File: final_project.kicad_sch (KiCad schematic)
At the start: 1 part, among them U1 ATmega328-P

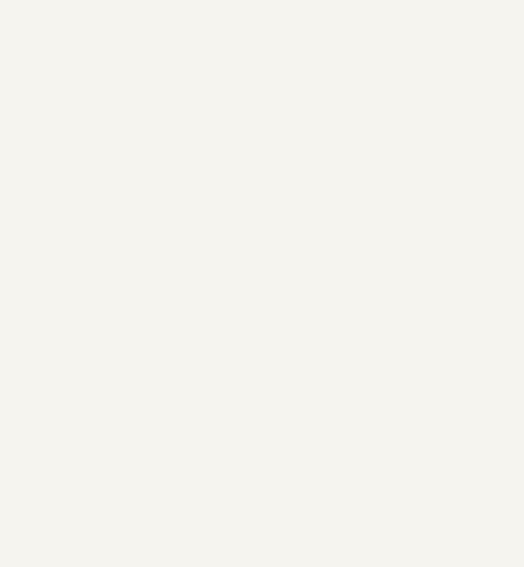
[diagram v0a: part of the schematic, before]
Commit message: Added SGP30 Sensor
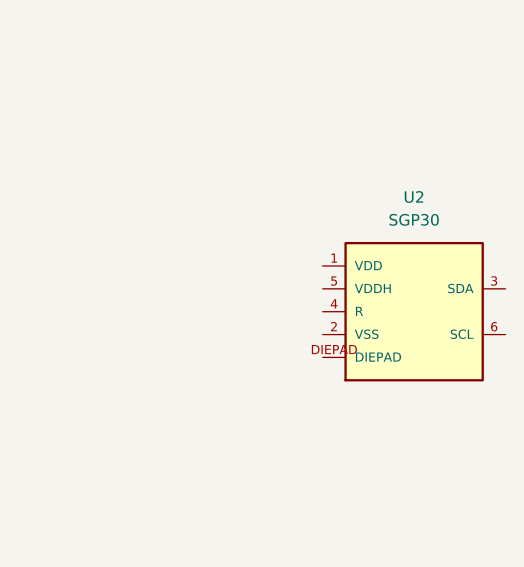
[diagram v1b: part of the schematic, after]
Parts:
- added U2: SGP30, SGP30:SGP30, symbol SGP30:SGP30
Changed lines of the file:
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@@
 	(paper "A4")
+	(symbol
+		(lib_id "SGP30:SGP30")
+		(at 158.75 87.63 0)
+		(unit 1)
+		(exclude_from_sim no)
+		(in_bom yes)
+		(on_board yes)
+		(dnp no)
+		(fields_autoplaced yes)
+		(property "Reference" "U2"
+			(at 158.75 74.93 0)
+			(effects
+				(font
+					(size 1.27 1.27)
+				)
+			)
+		)
+		(property "Value" "SGP30"
+			(at 158.75 77.47 0)
+			(effects
+				(font
+					(size 1.27 1.27)
+				)
+			)
+		)
+		(property "Footprint" "SGP30:SGP30"
+			(at 158.75 87.63 0)
+			(effects
+				(font
+					(size 1.27 1.27)
+				)
+				(justify bottom)
+				(hide yes)
+			)
+		)
+		(property "Datasheet" ""
+			(at 158.75 87.63 0)
+			(effects
+				(font
+					(size 1.27 1.27)
+				)
+				(hide yes)
+			)
+		)
+		(property "Description" ""
+			(at 158.75 87.63 0)
+			(effects
+				(font
+					(size 1.27 1.27)
+				)
+				(hide yes)
+			)
+		)
+		(property "MF" "Sensirion AG"
+			(at 158.75 87.63 0)
+			(effects
+				(font
+					(size 1.27 1.27)
+				)
+				(justify bottom)
+				(hide yes)
+			)
+		)
+		(property "Description_1" "SGP30, SHTC1 Air Quality, Humidity, Temperature Sensor Arduino Platform Evaluation Expansion Board"
+			(at 158.75 87.63 0)
+			(effects
+				(font
+					(size 1.27 1.27)
+				)
+				(justify bottom)
+				(hide yes)
+			)
+		)
+		(property "Package" "None"
+			(at 158.75 87.63 0)
+			(effects
+				(font
+					(size 1.27 1.27)
+				)
+				(justify bottom)
+				(hide yes)
+			)
+		)
+		(property "Price" "None"
+			(at 158.75 87.63 0)
+			(effects
+				(font
+					(size 1.27 1.27)
+				)
+				(justify bottom)
+				(hide yes)
+			)
+		)
+		(property "Check_prices" "https://www.snapeda.com/parts/SGP30/Sensirion/view-part/?ref=eda"
+			(at 158.75 87.63 0)
+			(effects
+				(font
+					(size 1.27 1.27)
+				)
+				(justify bottom)
+				(hide yes)
+			)
+		)
+		(property "VALUE" "SGP30"
+			(at 158.75 87.63 0)
+			(effects
+				(font
+					(size 1.27 1.27)
+				)
+				(justify bottom)
+				(hide yes)
+			)
+		)
+		(property "SnapEDA_Link" "https://www.snapeda.com/parts/SGP30/Sensirion/view-part/?ref=snap"
+			(at 158.75 87.63 0)
+			(effects
+				(font
+					(size 1.27 1.27)
+				)
+				(justify bottom)
+				(hide yes)
+			)
+		)
+		(property "PROD_ID" "IC-14776"
+			(at 158.75 87.63 0)
+			(effects
+				(font
+					(size 1.27 1.27)
+				)
+				(justify bottom)
+				(hide yes)
+			)
+		)
+		(property "Availability" "Not in stock"
+			(at 158.75 87.63 0)
+			(effects
+				(font
+					(size 1.27 1.27)
+				)
+				(justify bottom)
+				(hide yes)
+			)
+		)
+		(property "MP" "SGP30"
+			(at 158.75 87.63 0)
+			(effects
+				(font
+					(size 1.27 1.27)
+				)
+				(justify bottom)
+				(hide yes)
+			)
+		)
+		(pin "2"
+		)
+		(pin "3"
+		)
+		(pin "5"
+		)
+		(pin "1"
+		)
+		(pin "4"
+		)
+		(pin "DIEPAD"
+		)
+		(pin "6"
+		)
+		(instances
+			(project ""
+				(path "/69077819-e109-4340-8082-9c11186228b7"
+					(reference "U2")
+					(unit 1)
+				)
+			)
+		)
+	)
 	(symbol
 		(lib_id "MCU_Microchip_ATmega:ATmega328-P")

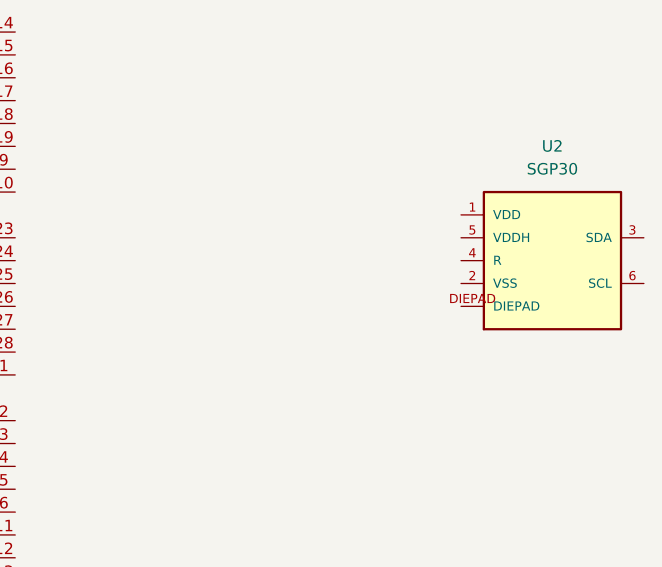
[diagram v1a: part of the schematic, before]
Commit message: Added GND to SGP30 sensor
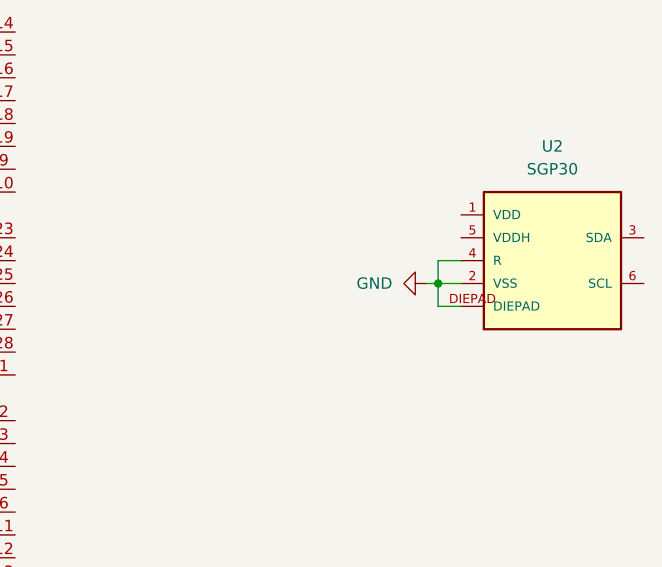
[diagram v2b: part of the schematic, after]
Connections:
- net GND: now reaches U2.2 (VSS)
- net GND: now also U2.4 (R), U2.DIEPAD
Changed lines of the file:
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@@
 	(generator_version "9.0")
 	(paper "A4")
+	(junction
+		(at 146.05 90.17)
+		(diameter 0)
+		(color 0 0 0 0)
+	)
+	(wire
+		(pts
+			(xy 146.05 90.17) (xy 148.59 90.17)
+		)
+		(stroke
+			(width 0)
+			(type default)
+		)
+	)
+	(wire
+		(pts
+			(xy 146.05 87.63) (xy 148.59 87.63)
+		)
+		(stroke
+			(width 0)
+			(type default)
+		)
+	)
+	(wire
+		(pts
+			(xy 146.05 90.17) (xy 146.05 92.71)
+		)
+		(stroke
+			(width 0)
+			(type default)
+		)
+	)
+	(wire
+		(pts
+			(xy 146.05 92.71) (xy 148.59 92.71)
+		)
+		(stroke
+			(width 0)
+			(type default)
+		)
+	)
+	(wire
+		(pts
+			(xy 146.05 90.17) (xy 146.05 87.63)
+		)
+		(stroke
+			(width 0)
+			(type default)
+		)
+	)
+	(wire
+		(pts
+			(xy 144.78 90.17) (xy 146.05 90.17)
+		)
+		(stroke
+			(width 0)
+			(type default)
+		)
+	)
+	(symbol
+		(lib_id "power:GND")
+		(at 144.78 90.17 270)
+		(unit 1)
+		(exclude_from_sim no)
+		(in_bom yes)
+		(on_board yes)
+		(dnp no)
+		(fields_autoplaced yes)
+		(property "Reference" "#PWR01"
+			(at 138.43 90.17 0)
+			(effects
+				(font
+					(size 1.27 1.27)
+				)
+				(hide yes)
+			)
+		)
+		(property "Value" "GND"
+			(at 140.97 90.1699 90)
+			(effects
+				(font
+					(size 1.27 1.27)
+				)
+				(justify right)
+			)
+		)
+		(property "Footprint" ""
+			(at 144.78 90.17 0)
+			(effects
+				(font
+					(size 1.27 1.27)
+				)
+				(hide yes)
+			)
+		)
+		(property "Datasheet" ""
+			(at 144.78 90.17 0)
+			(effects
+				(font
+					(size 1.27 1.27)
+				)
+				(hide yes)
+			)
+		)
+		(property "Description" "Power symbol creates a global label with name \"GND\" , ground"
+			(at 144.78 90.17 0)
+			(effects
+				(font
+					(size 1.27 1.27)
+				)
+				(hide yes)
+			)
+		)
+		(pin "1"
+		)
+		(instances
+			(project ""
+				(path "/69077819-e109-4340-8082-9c11186228b7"
+					(reference "#PWR01")
+					(unit 1)
+				)
+			)
+		)
+	)
 	(symbol
 		(lib_id "SGP30:SGP30")

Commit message: Updated PCB Design
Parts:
- added C1: 100nF, symbol Device:C
- added R1_Pullup, R2_Pullup: 10k, symbol Device:R
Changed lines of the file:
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@@
+	)
+	(symbol
+		(lib_id "Device:C")
+		(at 144.78 78.74 0)
+		(unit 1)
+		(exclude_from_sim no)
+		(in_bom yes)
+		(on_board yes)
+		(dnp no)
+		(fields_autoplaced yes)
+		(property "Reference" "C1"
+			(at 148.59 77.4699 0)
+			(effects
+				(font
+					(size 1.27 1.27)
+				)
+				(justify left)
+			)
+		)
+		(property "Value" "100nF"
+			(at 148.59 80.0099 0)
+			(effects
+				(font
+					(size 1.27 1.27)
+				)
+				(justify left)
+			)
+		)
+		(property "Footprint" ""
+			(at 145.7452 82.55 0)
+			(effects
+				(font
+					(size 1.27 1.27)
+				)
+				(hide yes)
+			)
+		)
+		(property "Datasheet" "~"
+			(at 144.78 78.74 0)
+			(effects
+				(font
+					(size 1.27 1.27)
+				)
+				(hide yes)
+			)
+		)
+		(property "Description" "Unpolarized capacitor"
+			(at 144.78 78.74 0)
+			(effects
+				(font
+					(size 1.27 1.27)
+				)
+				(hide yes)
+			)
+		)
+		(pin "2"
+		)
+		(pin "1"
+		)
+		(instances
+			(project ""
+				(path "/69077819-e109-4340-8082-9c11186228b7"
+					(reference "C1")
+					(unit 1)
+				)
+			)
+		)
 	)
 	(symbol
@@
 					(unit 1)
 				)
+			)
+		)
+	)
+	(symbol
+		(lib_id "Device:R")
+		(at 129.54 77.47 0)
+		(unit 1)
+		(exclude_from_sim no)
+		(in_bom yes)
+		(on_board yes)
+		(dnp no)
+		(fields_autoplaced yes)
+		(property "Reference" "R2_Pullup"
+			(at 132.08 76.1999 0)
+			(effects
+				(font
+					(size 1.27 1.27)
+				)
+				(justify left)
+			)
+		)
+		(property "Value" "10k"
+			(at 132.08 78.7399 0)
+			(effects
+				(font
+					(size 1.27 1.27)
+				)
+				(justify left)
+			)
+		)
+		(property "Footprint" ""
+			(at 127.762 77.47 90)
+			(effects
+				(font
+					(size 1.27 1.27)
+				)
+				(hide yes)
+			)
+		)
+		(property "Datasheet" "~"
+			(at 129.54 77.47 0)
+			(effects
+				(font
+					(size 1.27 1.27)
+				)
+				(hide yes)
+			)
+		)
+		(property "Description" "Resistor"
+			(at 129.54 77.47 0)
+			(effects
+				(font
+					(size 1.27 1.27)
+				)
+				(hide yes)
+			)
+		)
+		(pin "1"
+		)
+		(pin "2"
+		)
+		(instances
+			(project ""
+				(path "/69077819-e109-4340-8082-9c11186228b7"
+					(reference "R2_Pullup")
+					(unit 1)
+				)
+			)
+		)
+	)
+	(symbol
+		(lib_id "Device:R")
+		(at 175.26 77.47 0)
+		(unit 1)
+		(exclude_from_sim no)
+		(in_bom yes)
+		(on_board yes)
+		(dnp no)
+		(fields_autoplaced yes)
+		(property "Reference" "R1_Pullup"
+			(at 177.8 76.1999 0)
+			(effects
+				(font
+					(size 1.27 1.27)
+				)
+				(justify left)
+			)
+		)
+		(property "Value" "10k"
+			(at 177.8 78.7399 0)
+			(effects
+				(font
+					(size 1.27 1.27)
+				)
+				(justify left)
+			)
+		)
+		(property "Footprint" ""
+			(at 173.482 77.47 90)
+			(effects
+				(font
+					(size 1.27 1.27)
+				)
+				(hide yes)
+			)
+		)
+		(property "Datasheet" "~"
+			(at 175.26 77.47 0)
+			(effects
+				(font
+					(size 1.27 1.27)
+				)
+				(hide yes)
+			)
+		)
+		(property "Description" "Resistor"
+			(at 175.26 77.47 0)
+			(effects
+				(font
+					(size 1.27 1.27)
+				)
+				(hide yes)
+			)
+		)
+		(pin "2"
+		)
+		(pin "1"
+		)
+		(instances
+			(project ""
+				(path "/69077819-e109-4340-8082-9c11186228b7"
+					(reference "R1_Pullup")
+					(unit 1)
+				)

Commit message: Added Voltage Regulator
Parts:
- added C2_In, C3_Out: 1u, symbol Device:C
- added C4_NR: 10n, symbol Device:C
- added R1: 76.8k, symbol Device:R
- added R2: 147k, symbol Device:R
- added U3_5V_to_1.8V_Voltage_Regulator: ADP3336ARMZ, Package_SO:MSOP-8_3x3mm_P0.65mm, symbol Regulator_Linear:ADP3336ARMZ
- C1: value 100nF -> 100n
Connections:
- net GND: now also C2_In.2, C3_Out.2, R2.2, U3_5V_to_1.8V_Voltage_Regulator.4 (GND)
- net at C1.1: now also R1_Pullup.1, R2_Pullup.1, C3_Out.1, C4_NR.2, R1.2, U3_5V_to_1.8V_Voltage_Regulator.1 (OUT), U3_5V_to_1.8V_Voltage_Regulator.2 (OUT), U3_5V_to_1.8V_Voltage_Regulator.3 (OUT)
- net at C1.2: now also U2.1 (VDD)
- net at U2.3 (SDA): now also R1_Pullup.2
- net at U2.6 (SCL): now also R2_Pullup.2
- net at U1.7 (VCC): now also C2_In.1, U3_5V_to_1.8V_Voltage_Regulator.7 (IN), U3_5V_to_1.8V_Voltage_Regulator.8 (IN)
- new net: C4_NR.1, R1.1, R2.1, U3_5V_to_1.8V_Voltage_Regulator.5 (FB)
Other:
- moved on the sheet: C1, R1_Pullup, R2_Pullup, U2

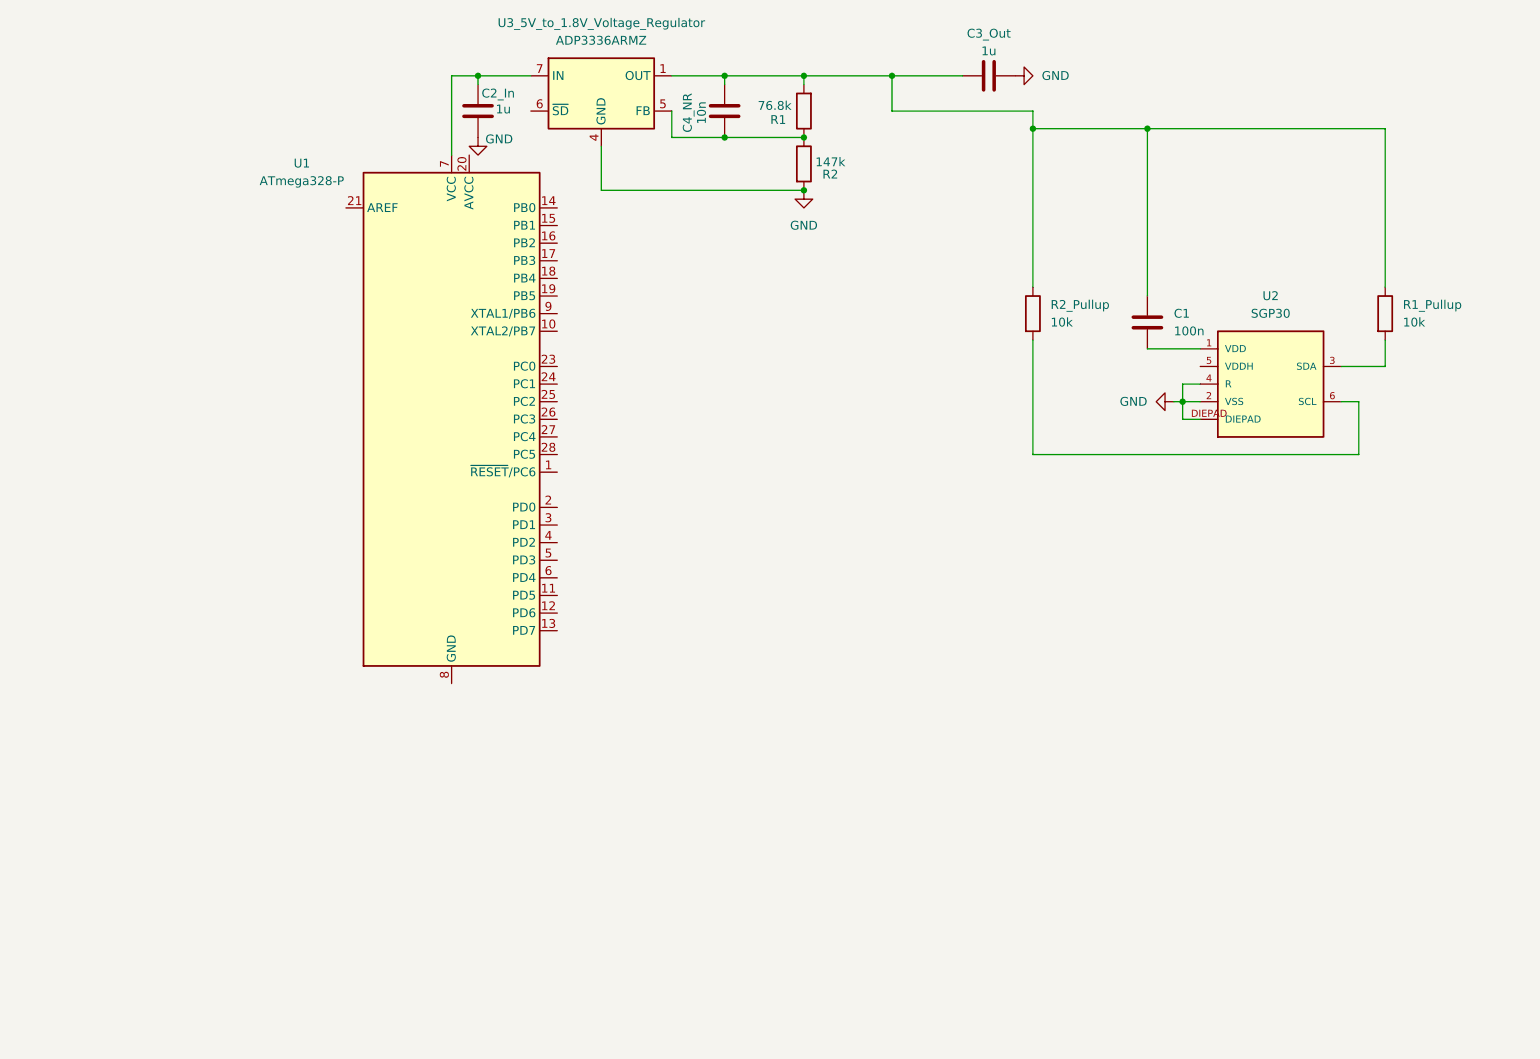
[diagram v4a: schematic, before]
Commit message: Added a bidirectional level shifter
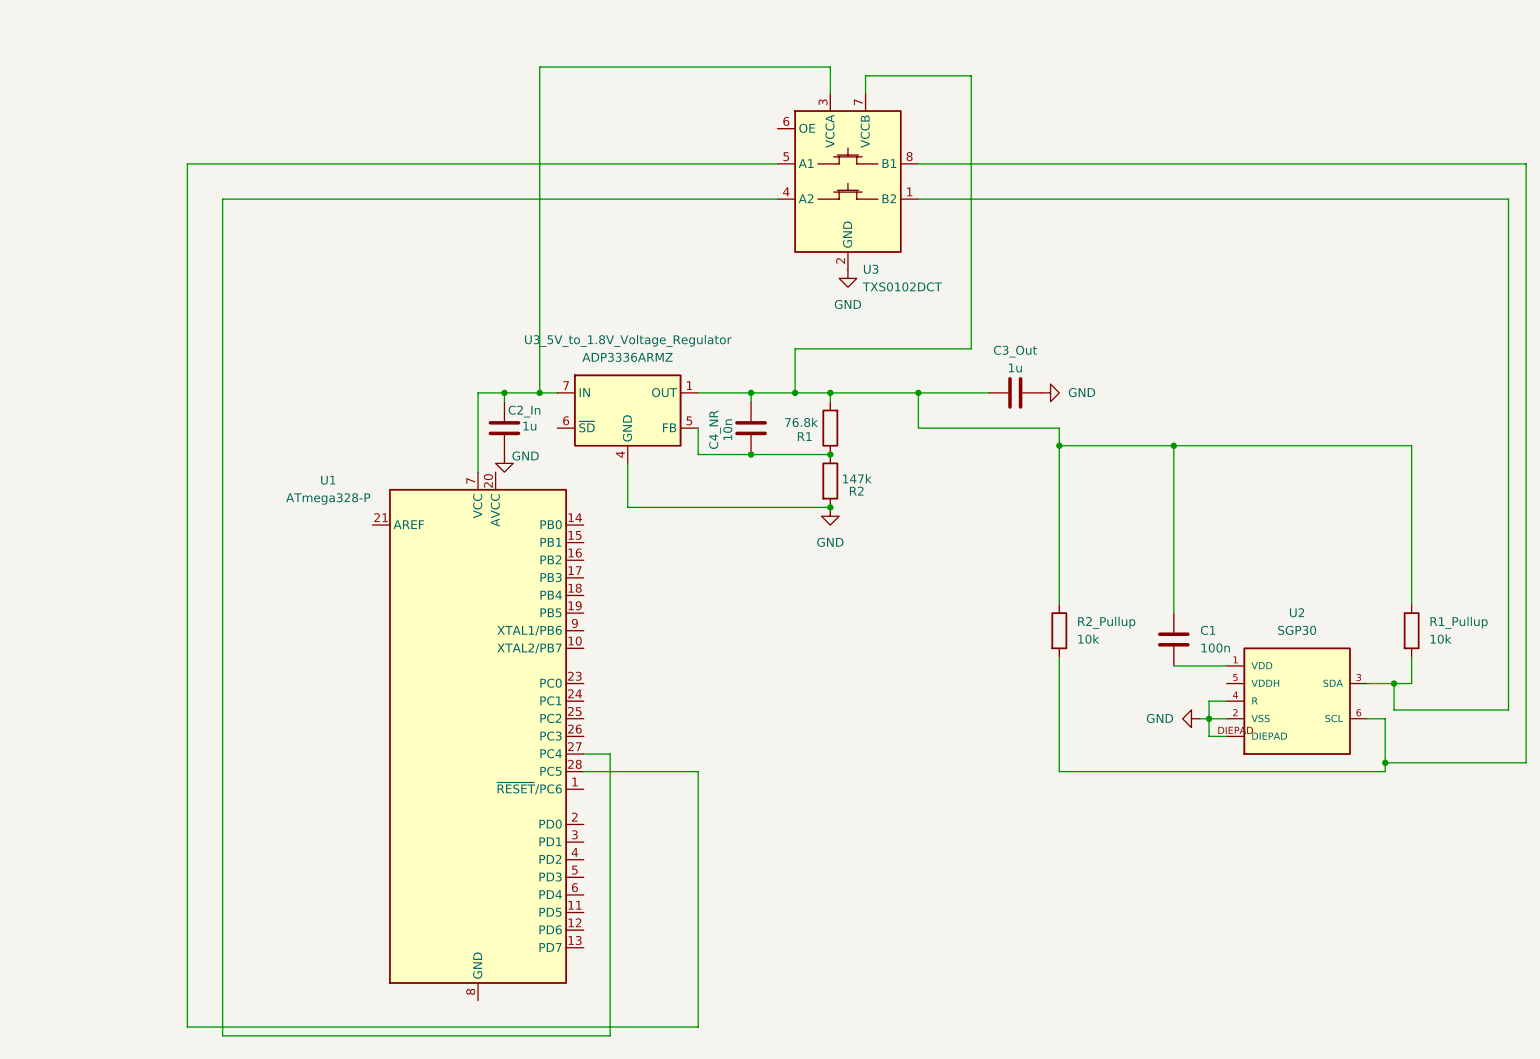
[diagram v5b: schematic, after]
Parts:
- added U3: TXS0102DCT, Package_SO:SSOP-8_2.95x2.8mm_P0.65mm, symbol Logic_LevelTranslator:TXS0102DCT
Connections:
- net GND: now also U3.2 (GND)
- net at C1.1, C3_Out.1, C4_NR.2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: now also U3.7 (VCCB)
- net at C2_In.1, U1.7 (VCC), U3_5V_to_1.8V_Voltage_Regulator.7 (IN)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: now also U3.3 (VCCA)
- net at R1_Pullup.2, U2.3 (SDA): now also U3.1 (B2)
- net at R2_Pullup.2, U2.6 (SCL): now also U3.8 (B1)
- net at U1.27 (PC4): now also U3.4 (A2)
- net at U1.28 (PC5): now also U3.5 (A1)
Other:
- moved on the sheet: C1, C2_In, C3_Out, C4_NR, R1, R1_Pullup, R2, R2_Pullup, U1, U2, U3_5V_to_1.8V_Voltage_Regulator
